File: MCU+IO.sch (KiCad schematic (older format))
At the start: 15 parts

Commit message: Did stuff
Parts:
- gave numbers to parts that had none: 15
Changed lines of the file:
@@
 P 4750 3925
 AR Path="/5FCE8B0A" Ref="U?"  Part="1"
-AR Path="/5FCCBFB4/5FCE8B0A" Ref="U?"  Part="1"
-F 0 "U?" H 4700 3950 50  0000 L CNN
+AR Path="/5FCCBFB4/5FCE8B0A" Ref="U2"  Part="1"
+F 0 "U2" H 4700 3950 50  0000 L CNN
 F 1 "WeMos_D1_mini" H 4800 3175 50  0000 L CNN
 F 2 "Module:WEMOS_D1_mini_light" H 4750 2775 50  0001 C CNN
@@
 P 4750 4725
 AR Path="/5FCE8B16" Ref="#PWR?"  Part="1"
-AR Path="/5FCCBFB4/5FCE8B16" Ref="#PWR?"  Part="1"
-F 0 "#PWR?" H 4750 4475 50  0001 C CNN
+AR Path="/5FCCBFB4/5FCE8B16" Ref="#PWR0102"  Part="1"
+F 0 "#PWR0102" H 4750 4475 50  0001 C CNN
 F 1 "GND" H 4755 4552 50  0000 C CNN
 F 2 "" H 4750 4725 50  0001 C CNN
@@
 P 5875 3475
 AR Path="/5FCE8B1C" Ref="R?"  Part="1"
-AR Path="/5FCCBFB4/5FCE8B1C" Ref="R?"  Part="1"
-F 0 "R?" H 5816 3429 50  0000 R CNN
+AR Path="/5FCCBFB4/5FCE8B1C" Ref="R2"  Part="1"
+F 0 "R2" H 5816 3429 50  0000 R CNN
 F 1 "4k7" H 5816 3520 50  0000 R CNN
 F 2 "Resistor_SMD:R_0603_1608Metric_Pad1.05x0.95mm_HandSolder" H 5875 3475 50  0001 C CNN
@@
 P 5975 3475
 AR Path="/5FCE8B22" Ref="R?"  Part="1"
-AR Path="/5FCCBFB4/5FCE8B22" Ref="R?"  Part="1"
-F 0 "R?" H 5916 3429 50  0000 R CNN
+AR Path="/5FCCBFB4/5FCE8B22" Ref="R3"  Part="1"
+F 0 "R3" H 5916 3429 50  0000 R CNN
 F 1 "4k7" H 5916 3520 50  0000 R CNN
 F 2 "Resistor_SMD:R_0603_1608Metric_Pad1.05x0.95mm_HandSolder" H 5975 3475 50  0001 C CNN
@@
 P 7400 3350
 AR Path="/5FCE8B42" Ref="D?"  Part="1"
-AR Path="/5FCCBFB4/5FCE8B42" Ref="D?"  Part="1"
-F 0 "D?" V 7475 3475 50  0000 R CNN
+AR Path="/5FCCBFB4/5FCE8B42" Ref="D2"  Part="1"
+F 0 "D2" V 7475 3475 50  0000 R CNN
 F 1 "VSML3710-GS18" V 7375 2650 50  0000 L CNN
 F 2 "LED_SMD:LED_PLCC-2" V 7400 3350 50  0001 C CNN
@@
 P 7400 3550
 AR Path="/5FCE8B48" Ref="R?"  Part="1"
-AR Path="/5FCCBFB4/5FCE8B48" Ref="R?"  Part="1"
-F 0 "R?" H 7459 3596 50  0000 L CNN
+AR Path="/5FCCBFB4/5FCE8B48" Ref="R4"  Part="1"
+F 0 "R4" H 7459 3596 50  0000 L CNN
 F 1 "6R8" H 7459 3505 50  0000 L CNN
 F 2 "Resistor_SMD:R_0603_1608Metric_Pad1.05x0.95mm_HandSolder" H 7400 3550 50  0001 C CNN
@@
 P 7525 4300
 AR Path="/5FCE8B4E" Ref="#PWR?"  Part="1"
-AR Path="/5FCCBFB4/5FCE8B4E" Ref="#PWR?"  Part="1"
-F 0 "#PWR?" H 7525 4050 50  0001 C CNN
+AR Path="/5FCCBFB4/5FCE8B4E" Ref="#PWR0103"  Part="1"
+F 0 "#PWR0103" H 7525 4050 50  0001 C CNN
 F 1 "GND" H 7530 4127 50  0000 C CNN
 F 2 "" H 7525 4300 50  0001 C CNN
@@
 P 7425 3950
 AR Path="/5FCE8B54" Ref="Q?"  Part="1"
-AR Path="/5FCCBFB4/5FCE8B54" Ref="Q?"  Part="1"
-F 0 "Q?" H 7630 3996 50  0000 L CNN
+AR Path="/5FCCBFB4/5FCE8B54" Ref="Q1"  Part="1"
+F 0 "Q1" H 7630 3996 50  0000 L CNN
 F 1 "FDN339AN" H 7125 3800 50  0000 L CNN
 F 2 "Package_TO_SOT_SMD:SOT-23_Handsoldering" H 7625 4050 50  0001 C CNN
@@
 P 6975 4100
 AR Path="/5FCE8B5A" Ref="R?"  Part="1"
-AR Path="/5FCCBFB4/5FCE8B5A" Ref="R?"  Part="1"
-F 0 "R?" H 6916 4054 50  0000 R CNN
+AR Path="/5FCCBFB4/5FCE8B5A" Ref="R7"  Part="1"
+F 0 "R7" H 6916 4054 50  0000 R CNN
 F 1 "4k7" H 6916 4145 50  0000 R CNN
 F 2 "Resistor_SMD:R_0603_1608Metric_Pad1.05x0.95mm_HandSolder" H 6975 4100 50  0001 C CNN
@@
 P 7125 3950
 AR Path="/5FCE8B60" Ref="R?"  Part="1"
-AR Path="/5FCCBFB4/5FCE8B60" Ref="R?"  Part="1"
-F 0 "R?" V 6929 3950 50  0000 C CNN
+AR Path="/5FCCBFB4/5FCE8B60" Ref="R6"  Part="1"
+F 0 "R6" V 6929 3950 50  0000 C CNN
 F 1 "1k" V 7020 3950 50  0000 C CNN
 F 2 "Resistor_SMD:R_0603_1608Metric_Pad1.05x0.95mm_HandSolder" H 7125 3950 50  0001 C CNN
@@
 P 7650 3350
 AR Path="/5FCE8B74" Ref="D?"  Part="1"
-AR Path="/5FCCBFB4/5FCE8B74" Ref="D?"  Part="1"
-F 0 "D?" V 7725 3300 50  0000 R CNN
+AR Path="/5FCCBFB4/5FCE8B74" Ref="D3"  Part="1"
+F 0 "D3" V 7725 3300 50  0000 R CNN
 F 1 "VSML3710-GS18" V 7700 4300 50  0000 R CNN
 F 2 "LED_SMD:LED_PLCC-2" V 7650 3350 50  0001 C CNN
@@
 P 7650 3550
 AR Path="/5FCE8B7A" Ref="R?"  Part="1"
-AR Path="/5FCCBFB4/5FCE8B7A" Ref="R?"  Part="1"
-F 0 "R?" H 7709 3596 50  0000 L CNN
+AR Path="/5FCCBFB4/5FCE8B7A" Ref="R5"  Part="1"
+F 0 "R5" H 7709 3596 50  0000 L CNN
 F 1 "6R8" H 7709 3505 50  0000 L CNN
 F 2 "Resistor_SMD:R_0603_1608Metric_Pad1.05x0.95mm_HandSolder" H 7650 3550 50  0001 C CNN
@@
 P 3525 3225
 AR Path="/5FCE8B9B" Ref="R?"  Part="1"
-AR Path="/5FCCBFB4/5FCE8B9B" Ref="R?"  Part="1"
-F 0 "R?" H 3466 3179 50  0000 R CNN
+AR Path="/5FCCBFB4/5FCE8B9B" Ref="R1"  Part="1"
+F 0 "R1" H 3466 3179 50  0000 R CNN
 F 1 "10k" H 3466 3270 50  0000 R CNN
 F 2 "Resistor_SMD:R_0603_1608Metric_Pad1.05x0.95mm_HandSolder" H 3525 3225 50  0001 C CNN
@@
 P 3175 3825
 AR Path="/5FCE8BB7" Ref="#PWR?"  Part="1"
-AR Path="/5FCCBFB4/5FCE8BB7" Ref="#PWR?"  Part="1"
-F 0 "#PWR?" H 3175 3575 50  0001 C CNN
+AR Path="/5FCCBFB4/5FCE8BB7" Ref="#PWR0104"  Part="1"
+F 0 "#PWR0104" H 3175 3575 50  0001 C CNN
 F 1 "GND" H 3180 3652 50  0000 C CNN
 F 2 "" H 3175 3825 50  0001 C CNN
@@
 P 3175 3225
 AR Path="/5FCE8BBD" Ref="C?"  Part="1"
-AR Path="/5FCCBFB4/5FCE8BBD" Ref="C?"  Part="1"
-F 0 "C?" H 3267 3271 50  0000 L CNN
+AR Path="/5FCCBFB4/5FCE8BBD" Ref="C1"  Part="1"
+F 0 "C1" H 3267 3271 50  0000 L CNN
 F 1 "1uF" H 3267 3180 50  0000 L CNN
 F 2 "Capacitor_SMD:C_0603_1608Metric_Pad1.05x0.95mm_HandSolder" H 3175 3225 50  0001 C CNN
@@
 P 3175 3625
 AR Path="/5FCE8BC3" Ref="SW?"  Part="1"
-AR Path="/5FCCBFB4/5FCE8BC3" Ref="SW?"  Part="1"
-F 0 "SW?" V 3221 3537 50  0000 R CNN
+AR Path="/5FCCBFB4/5FCE8BC3" Ref="SW1"  Part="1"
+F 0 "SW1" V 3221 3537 50  0000 R CNN
 F 1 "SW_SPST" V 3130 3537 50  0000 R CNN
 F 2 "Button_Switch_SMD:SW_Push_1P1T_NO_6x6mm_H9.5mm" H 3175 3625 50  0001 C CNN
@@
 P 3000 3050
 AR Path="/5FCE8BCF" Ref="D?"  Part="1"
-AR Path="/5FCCBFB4/5FCE8BCF" Ref="D?"  Part="1"
-F 0 "D?" H 3050 2950 50  0000 R CNN
+AR Path="/5FCCBFB4/5FCE8BCF" Ref="D1"  Part="1"
+F 0 "D1" H 3050 2950 50  0000 R CNN
 F 1 "BAT54WS" H 3175 2875 50  0000 R CNN
 F 2 "Diode_SMD:D_SOD-323_HandSoldering" V 3000 3050 50  0001 C CNN
@@
 P 8475 4050
 AR Path="/5FCE8BA7" Ref="#PWR?"  Part="1"
-AR Path="/5FCCBFB4/5FCE8BA7" Ref="#PWR?"  Part="1"
-F 0 "#PWR?" H 8475 3800 50  0001 C CNN
+AR Path="/5FCCBFB4/5FCE8BA7" Ref="#PWR0105"  Part="1"
+F 0 "#PWR0105" H 8475 3800 50  0001 C CNN
 F 1 "GND" H 8480 3877 50  0000 C CNN
 F 2 "" H 8475 4050 50  0001 C CNN
@@
 P 8925 3800
 AR Path="/5FCE8B8C" Ref="U?"  Part="1"
-AR Path="/5FCCBFB4/5FCE8B8C" Ref="U?"  Part="1"
-F 0 "U?" H 8975 4125 50  0000 R CNN
+AR Path="/5FCCBFB4/5FCE8B8C" Ref="U1"  Part="1"
+F 0 "U1" H 8975 4125 50  0000 R CNN
 F 1 "TSOP38236" H 9125 3500 50  0000 R CNN
 F 2 "OptoDevice:Vishay_MINICAST-3Pin" H 8875 3425 50  0001 C CNN

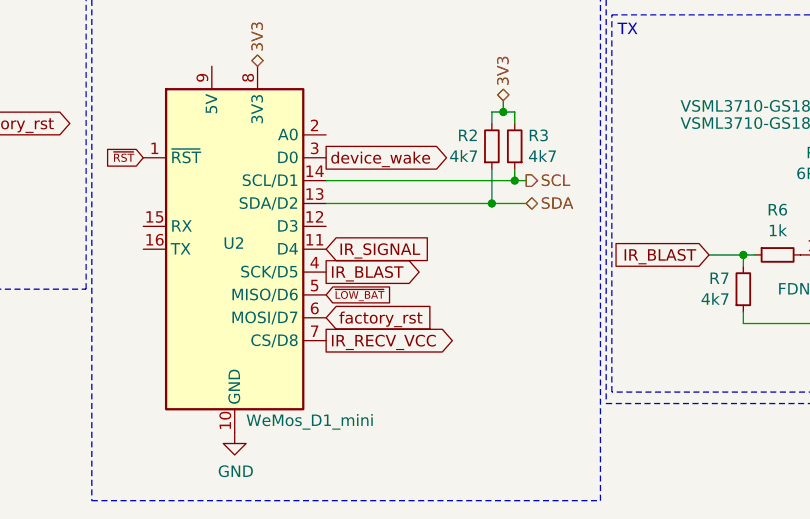
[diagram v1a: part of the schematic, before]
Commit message: Redesigned to small-stick formfactor
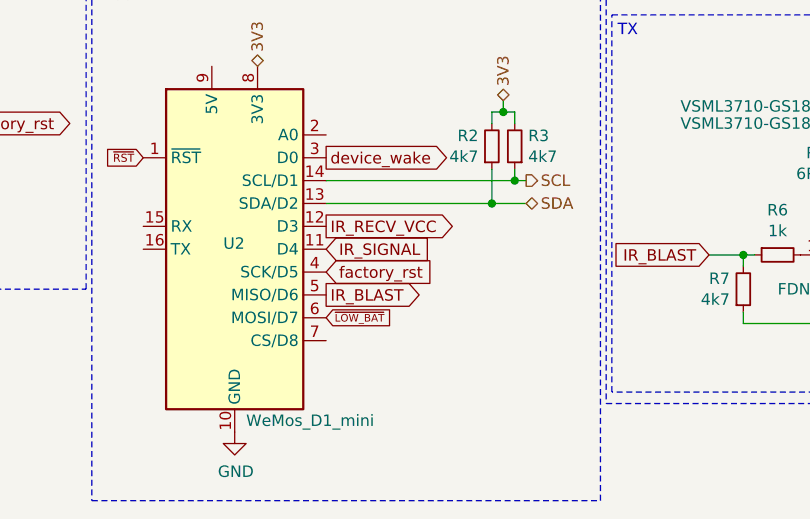
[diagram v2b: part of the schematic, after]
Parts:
- Q1: footprint Package_TO_SOT_SMD:SOT-23_Handsoldering -> Package_TO_SOT_SMD:SOT-23
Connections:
- net IR_BLAST: now also U2.5 (MISO/D6); no longer U2.4 (SCK/D5)
- net IR_RECV_VCC: now also U2.12 (D3); no longer U2.7 (CS/D8)
- net factory_rst: now also U2.4 (SCK/D5); no longer U2.6 (MOSI/D7)
- net ~LOW_BAT: now also U2.6 (MOSI/D7); no longer U2.5 (MISO/D6)
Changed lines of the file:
@@
 Text GLabel 5150 3525 2    50   Output ~ 0
 device_wake
-Text GLabel 5150 4025 2    50   Output ~ 0
+Text GLabel 5150 4125 2    50   Output ~ 0
 IR_BLAST
 Text GLabel 5150 3925 2    50   Input ~ 0
 IR_SIGNAL
-Text GLabel 5150 4325 2    50   Output ~ 0
+Text GLabel 5150 3825 2    50   Output ~ 0
 IR_RECV_VCC
-Text GLabel 5150 4225 2    50   Input ~ 0
+Text GLabel 5150 4025 2    50   Input ~ 0
 factory_rst
 Text GLabel 4350 3525 0    35   Input ~ 0
 ~RST
-Text GLabel 5150 4125 2    33   Input ~ 0
+Text GLabel 5150 4225 2    33   Input ~ 0
 ~LOW_BAT
 $Comp
@@
 F 0 "Q1" H 7630 3996 50  0000 L CNN
 F 1 "FDN339AN" H 7125 3800 50  0000 L CNN
-F 2 "Package_TO_SOT_SMD:SOT-23_Handsoldering" H 7625 4050 50  0001 C CNN
+F 2 "Package_TO_SOT_SMD:SOT-23" H 7625 4050 50  0001 C CNN
 F 3 "~" H 7425 3950 50  0001 C CNN
 	1    7425 3950

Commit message: Added stuff
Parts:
- added C1: 1uF, Capacitor_SMD:C_0603_1608Metric_Pad1.05x0.95mm_HandSolder, symbol Device:C_Small
- added U9: LM75C, Package_SO:SOIC-8_3.9x4.9mm_P1.27mm, symbol Sensor_Temperature:LM75C
- renumbered C1 to C11
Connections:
- net 3V3: now also C1.1, U9.5 (A2), U9.6 (A1), U9.7 (A0), U9.8 (+Vs)
- net GND: now also C1.2, U9.4 (GND)
- net SCL: now also U9.2 (SCL)
- net SDA: now also U9.1 (SDA)
- net ~LOW_BAT: now also U2.7 (CS/D8); no longer U2.6 (MOSI/D7)
- new net Temp_O.S.: U2.6 (MOSI/D7), U9.3 (O.S.)
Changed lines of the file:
@@
 Text GLabel 4350 3525 0    35   Input ~ 0
 ~RST
-Text GLabel 5150 4225 2    33   Input ~ 0
+Text GLabel 5150 4325 2    33   Input ~ 0
 ~LOW_BAT
 $Comp
@@
 P 3175 3225
 AR Path="/5FCE8BBD" Ref="C?"  Part="1"
-AR Path="/5FCCBFB4/5FCE8BBD" Ref="C1"  Part="1"
-F 0 "C1" H 3267 3271 50  0000 L CNN
+AR Path="/5FCCBFB4/5FCE8BBD" Ref="C11"  Part="1"
+F 0 "C11" H 3267 3271 50  0000 L CNN
 F 1 "1uF" H 3267 3180 50  0000 L CNN
 F 2 "Capacitor_SMD:C_0603_1608Metric_Pad1.05x0.95mm_HandSolder" H 3175 3225 50  0001 C CNN
@@
 Text HLabel 7525 3150 1    50   BiDi ~ 0
 3V3
+$Comp
+L Sensor_Temperature:LM75C U9
+U 1 1 5F6438DE
+P 7575 5625
+F 0 "U9" H 7350 6075 50  0000 C CNN
+F 1 "LM75C" H 7750 6075 50  0000 C CNN
+F 2 "Package_SO:SOIC-8_3.9x4.9mm_P1.27mm" H 7575 5625 50  0001 C CNN
+F 3 "http://www.ti.com/lit/ds/symlink/lm75b.pdf" H 7575 5625 50  0001 C CNN
+	1    7575 5625
+	1    0    0    -1
+$EndComp
+Text HLabel 7575 5025 1    50   BiDi ~ 0
+3V3
+$Comp
+L power:GND #PWR?
+U 1 1 5F647668
+P 7575 6225
+AR Path="/5F647668" Ref="#PWR?"  Part="1"
+AR Path="/5FCCBFB4/5F647668" Ref="#PWR0110"  Part="1"
+F 0 "#PWR0110" H 7575 5975 50  0001 C CNN
+F 1 "GND" H 7580 6052 50  0000 C CNN
+F 2 "" H 7575 6225 50  0001 C CNN
+F 3 "" H 7575 6225 50  0001 C CNN
+	1    7575 6225
+	1    0    0    -1
+$EndComp
+Wire Wire Line
+	7575 5025 7575 5075
+Wire Wire Line
+	7575 5075 8025 5075
+Wire Wire Line
+	8025 5075 8025 5525
+Wire Wire Line
+	8025 5725 7975 5725
+Connection ~ 7575 5075
+Wire Wire Line
+	7575 5075 7575 5125
+Wire Wire Line
+	7975 5625 8025 5625
+Connection ~ 8025 5625
+Wire Wire Line
+	8025 5625 8025 5725
+Wire Wire Line
+	7975 5525 8025 5525
+Connection ~ 8025 5525
+Wire Wire Line
+	8025 5525 8025 5625
+Text HLabel 7175 5525 0    50   BiDi ~ 0
+SDA
+Text HLabel 7175 5625 0    50   Output ~ 0
+SCL
+$Comp
+L Device:C_Small C?
+U 1 1 5F64E573
+P 8200 5625
+AR Path="/5F64E573" Ref="C?"  Part="1"
+AR Path="/5FCCBFB4/5F64E573" Ref="C1"  Part="1"
+F 0 "C1" H 8292 5671 50  0000 L CNN
+F 1 "1uF" H 8292 5580 50  0000 L CNN
+F 2 "Capacitor_SMD:C_0603_1608Metric_Pad1.05x0.95mm_HandSolder" H 8200 5625 50  0001 C CNN
+F 3 "~" H 8200 5625 50  0001 C CNN
+	1    8200 5625
+	1    0    0    -1
+$EndComp
+Wire Wire Line
+	7575 6225 7575 6175
+Wire Wire Line
+	7575 6175 8200 6175
+Wire Wire Line
+	8200 6175 8200 5725
+Connection ~ 7575 6175
+Wire Wire Line
+	7575 6175 7575 6125
+Wire Wire Line
+	8200 5525 8200 5075
+Wire Wire Line
+	8200 5075 8025 5075
+Connection ~ 8025 5075
+Text HLabel 7175 5725 0    50   UnSpc ~ 0
+Temp_O.S.
+Text HLabel 5150 4225 2    50   UnSpc ~ 0
+Temp_O.S.
 $EndSCHEMATC
